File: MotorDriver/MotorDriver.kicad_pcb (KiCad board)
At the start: 2 copper layers, 70 x 70 mm, 95 parts, among them J1 Conn_01x01, J2 Conn_01x01, J3 Conn_01x01, J4 Conn_01x01, J5 Conn_02x05_Odd_Even, J6 Conn_02x03_Odd_Even, J7 4P4C, J8 4P4C, Q1 Q_NMOS_GDS, Q2 Q_NMOS_GDS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

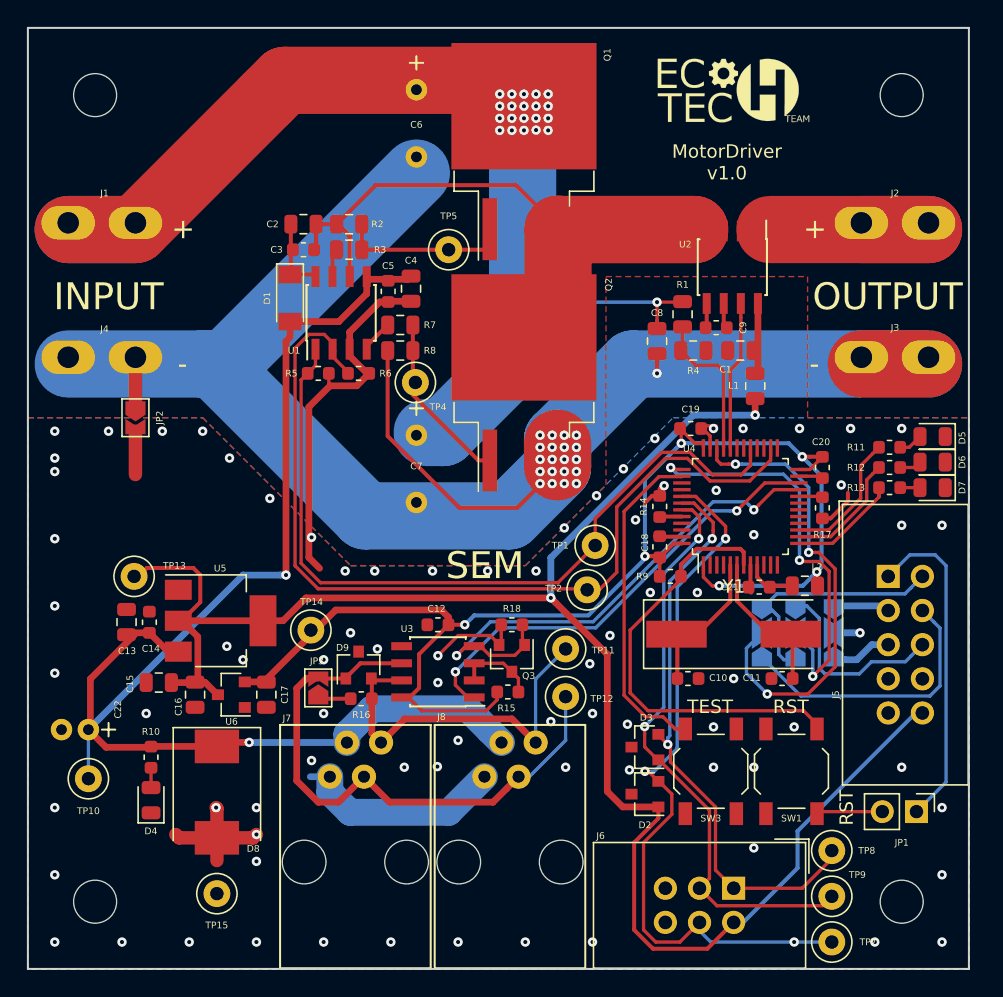
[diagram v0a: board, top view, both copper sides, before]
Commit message: Added version date on silk screen and changed signal tracks width to 0,2.
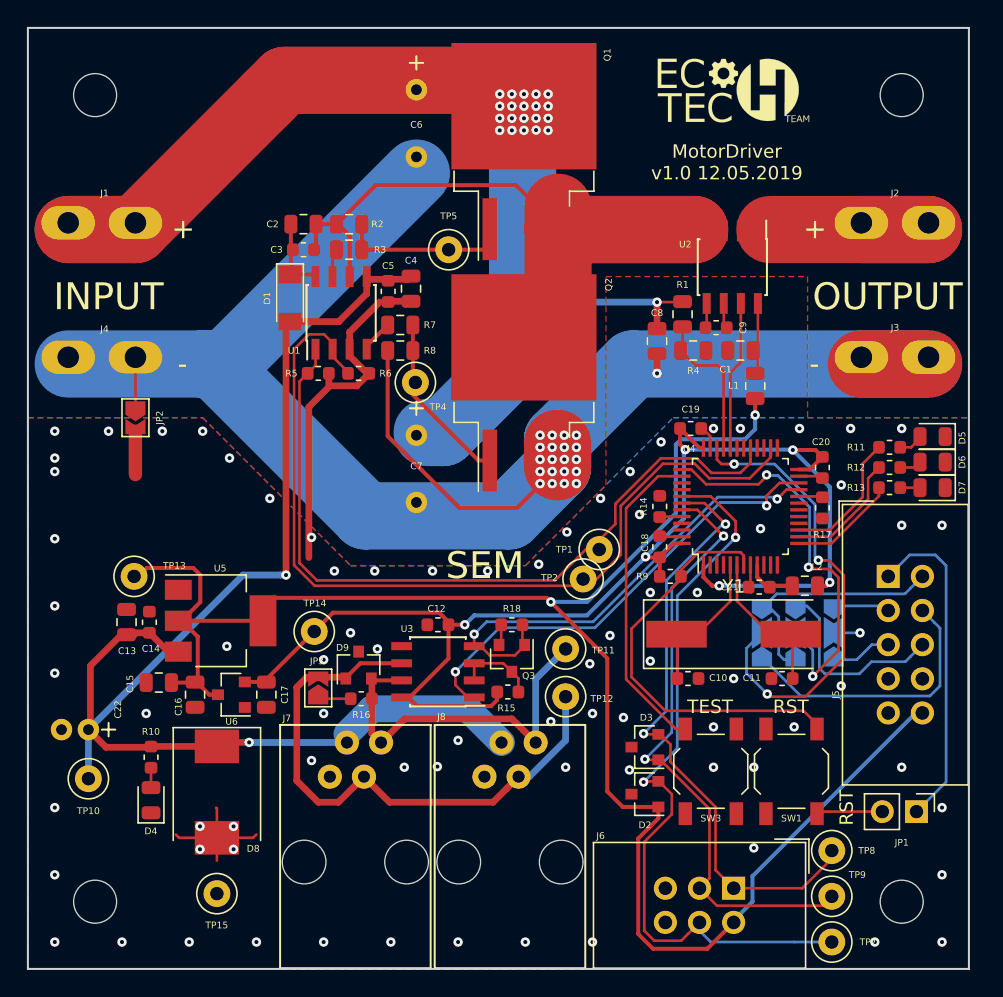
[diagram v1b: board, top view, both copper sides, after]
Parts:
- moved TP2 0.85 mm to (141.3, 111.5)
- moved TP1 0.42 mm to (142.5, 109.3)
- moved TP14 0.27 mm to (121.3, 115.4)
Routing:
- net GND: track 83.0 -> 54.1 mm, vias 82 -> 79
- net /TX: track 39.1 -> 36.0 mm
- net /ENCB: track 43.4 -> 45.9 mm
- net /ENCA: track 43.9 -> 46.1 mm
- net Net-(C6-Pad1): track 86.7 -> 84.7 mm
- net +5V: track 133.2 -> 134.8 mm
- net /RST: track 37.8 -> 36.4 mm
- net /ENCI: track 54.8 -> 56.2 mm, vias 3 -> 2
- net /LIN: track 67.8 -> 66.7 mm
- net /SWCLK: track 31.3 -> 30.2 mm
- net Net-(SW3-Pad1): track 24.7 -> 23.8 mm
- net /RX: track 34.1 -> 34.8 mm
- net +3V3: track 103.7 -> 104.3 mm
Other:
- net class 12V added: clearance 0.2, trace_width 0.5, via_dia 0.7, via_drill 0.3
- net class 3V3 added: clearance 0.2, trace_width 0.3, via_dia 0.7, via_drill 0.3
- net class 5V added: clearance 0.2, trace_width 0.3, via_dia 0.7, via_drill 0.3
- net class POWER added: clearance 0.2, trace_width 5, via_dia 0.7, via_drill 0.3
- net class RS485 added: clearance 0.2, trace_width 0.5, via_dia 0.7, via_drill 0.3
- board text added: "MotorDriver v1.0 12.05.2019"
- board text removed: "MotorDriver v1.0"
